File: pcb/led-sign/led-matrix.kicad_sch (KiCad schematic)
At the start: 42 parts, among them J1 USB_C_Receptacle, J2 Conn_01x03_Socket, Q1 PMOS, SW1 SW_Push, U1 nRF52832-QFxx, U2 TP4056-42-ESOP8, U3 LP5907MFX-3.3, U4 LP5024, U5 LP5024, Y1 32MHz

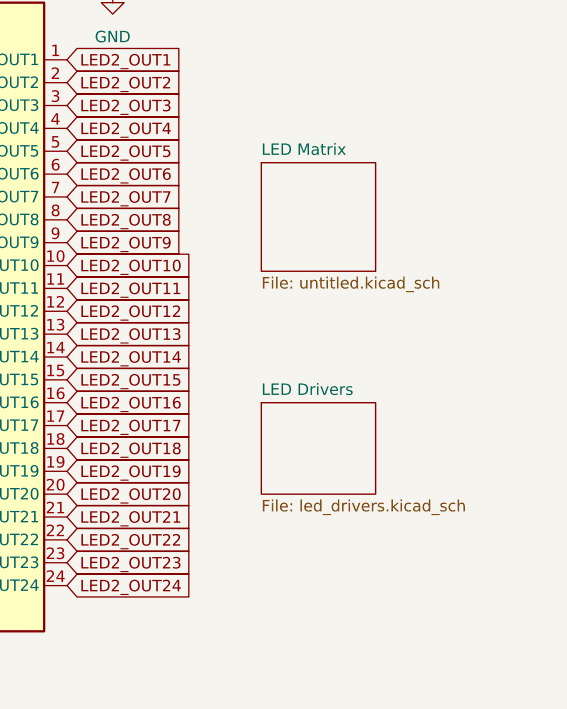
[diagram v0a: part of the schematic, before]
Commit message: add led matrix
Signed-off-by: 3nt3 <gott@3nt3.de>
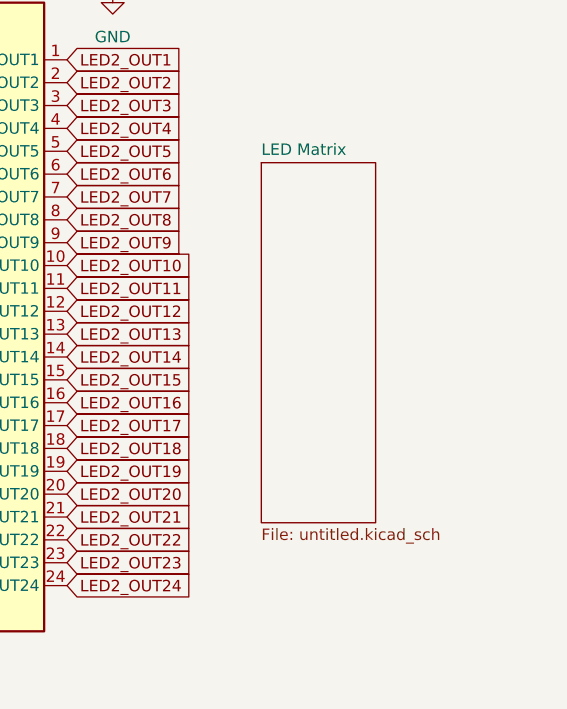
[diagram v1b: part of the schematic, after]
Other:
- removed sheet LED Drivers
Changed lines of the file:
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@@
 	(sheet
 		(at 381 157.48)
-		(size 12.7 12.065)
+		(size 12.7 40.005)
 		(exclude_from_sim no)
 		(in_bom yes)
@@
 		)
 		(property "Sheetfile" "untitled.kicad_sch"
-			(at 381 170.1296 0)
+			(at 381 198.0696 0)
 			(effects
 				(font
@@
 				)
 			)
-		)
-	)
-	(sheet
-		(at 381 184.15)
-		(size 12.7 10.16)
-		(exclude_from_sim no)
-		(in_bom yes)
-		(on_board yes)
-		(dnp no)
-		(fields_autoplaced yes)
-		(stroke
-			(width 0.1524)
-			(type solid)
-		)
-		(fill
-			(color 0 0 0 0.0000)
-		)
-		(property "Sheetname" "LED Drivers"
-			(at 381 183.4384 0)
-			(effects
-				(font
-					(size 1.27 1.27)
-				)
-				(justify left bottom)
-			)
-		)
-		(property "Sheetfile" "led_drivers.kicad_sch"
-			(at 381 194.8946 0)
-			(effects
-				(font
-					(size 1.27 1.27)
-				)
-				(justify left top)
-			)
-		)
-		(property "Field2" ""
-			(at 381 184.15 0)
-			(effects
-				(font
-					(size 1.27 1.27)
-				)
-			)
-		)
-		(instances
-			(project "led-sign"
-				(path "/e425a5d8-1381-45ac-b0d7-4099e608a776"
-					(page "3")
-				)
-			)
